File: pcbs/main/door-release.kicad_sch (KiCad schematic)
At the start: 7 parts

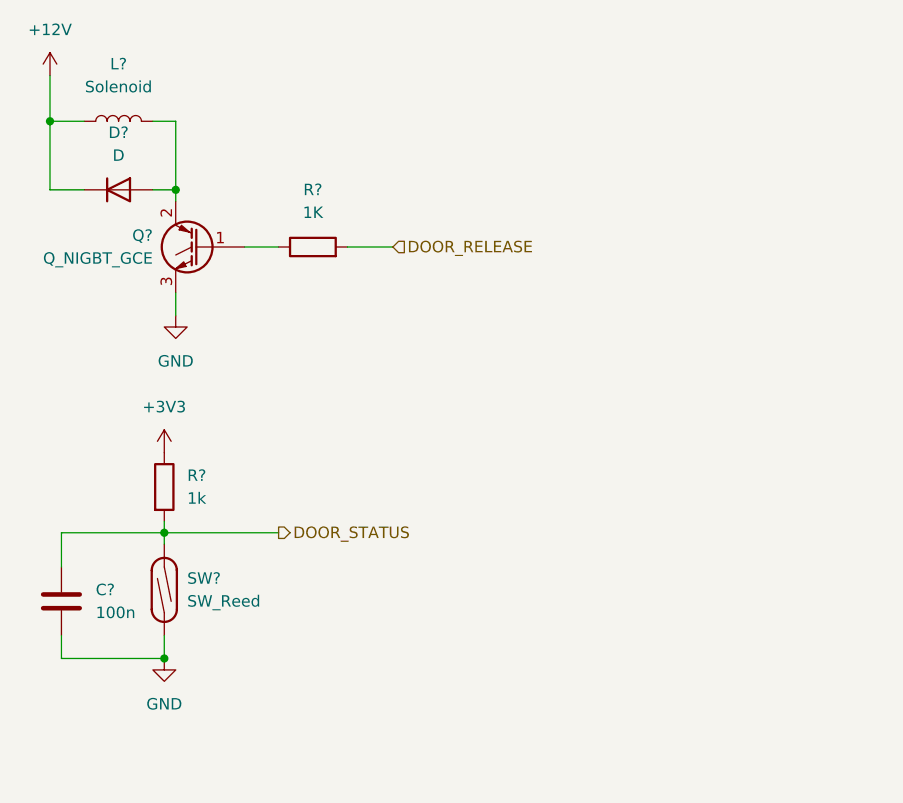
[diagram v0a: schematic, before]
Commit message: Change pull-up method on door status sensor
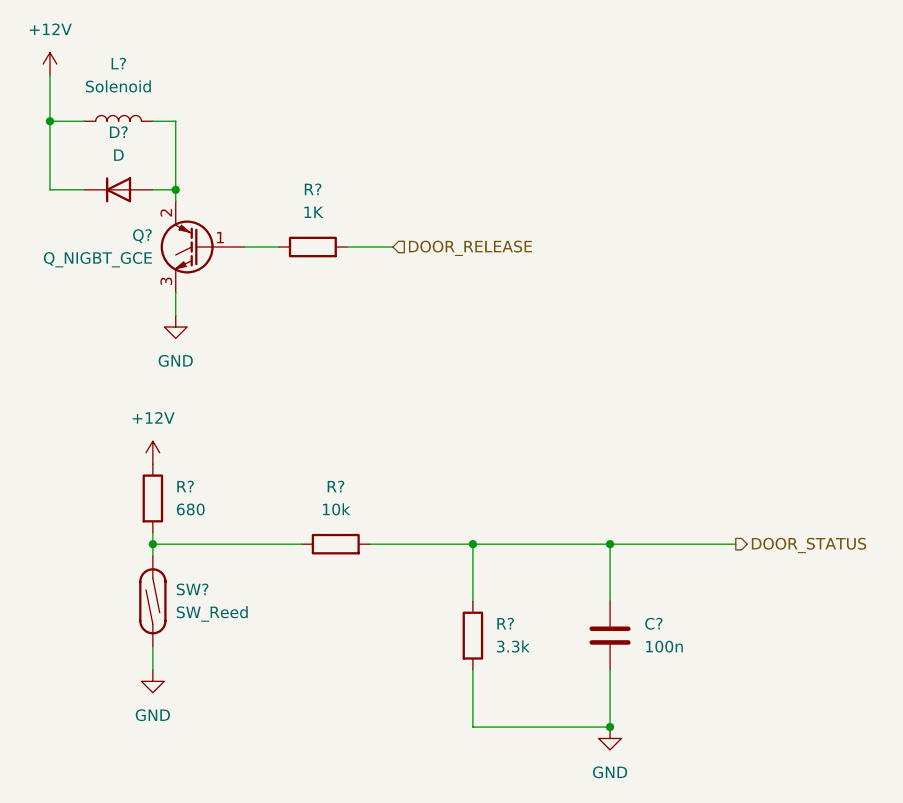
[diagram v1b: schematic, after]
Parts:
- added R?: 10k, symbol Device:R
- added R?: 3.3k, symbol Device:R
- R?: value 1k -> 680
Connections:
- net +3V3 is gone; now on net +12V: R?.1
- net DOOR_STATUS: now also R?.1, R?.2; no longer R?.2, SW?.2
- net GND: now also R?.2
- new net: R?.1, R?.2, SW?.2
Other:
- moved on the sheet: C?, R?, SW?
